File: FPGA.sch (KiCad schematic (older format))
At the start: 9 parts, among them U34 PCA9555AHF,128, U39 PCA9555AHF,128

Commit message: I2C voltage translator added, rotated POE bridges, I2C connected to SODIMM, NMOS for power leds indicator, 3V3P connected to SI570 and SODIMM
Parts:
- added C412, C415: CC0201_100NF_6.3V_10%_X5R, CAPC0603X33N, symbol Capacitors_SMD:CC0201_100NF_6.3V_10%_X5R
- added R25, R28: R0402_2K2_1%_0.0625W_100PPM, RESC1005X40N, symbol Resistors_SMD:R0402_2K2_1%_0.0625W_100PPM
- added U59: TCA9517DGKR, ICs And Semiconductors SMD:SOP65P490X110-8N, symbol Analog_&_Interface:TCA9517DGKR
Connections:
- net labels added: +3.3P, I2C_APP_3V3_SCL, I2C_APP_3V3_SDA
- wire segments 171 -> 187
- no-connect marks 12 -> 13

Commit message: More consistent attributes for LEDs and BSS138
Should match Marble-Mini
Fewer complaints from KiBoM
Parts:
- LD13, LD14: Manufacturer KINGBRIGHT -> WURTH; Manufacturer Part Number KPH-1608CGCK -> 150060VS75000
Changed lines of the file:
@@
 F 14 "~~" H 9750 8600 60  0001 L CNN "Status"
 F 15 "SMD Green LED, Case 1.6mmX0.8mm(0603), 0.65mm Thickness" H 9750 8510 60  0001 L CNN "Part Description"
-F 16 "KINGBRIGHT" H 9750 8420 60  0001 L CNN "Manufacturer"
-F 17 "KPH-1608CGCK" H 9750 8330 60  0001 L CNN "Manufacturer Part Number"
+F 16 "WURTH" H 9750 8420 60  0001 L CNN "Manufacturer"
+F 17 "150060VS75000" H 9750 8330 60  0001 L CNN "Manufacturer Part Number"
 F 18 "2" H 9750 8240 60  0001 L CNN "Pin Count"
 F 19 "~~" H 9750 8150 60  0001 L CNN "Case"
@@
 F 14 "~~" H 10100 8600 60  0001 L CNN "Status"
 F 15 "SMD Green LED, Case 1.6mmX0.8mm(0603), 0.65mm Thickness" H 10100 8510 60  0001 L CNN "Part Description"
-F 16 "KINGBRIGHT" H 10100 8420 60  0001 L CNN "Manufacturer"
-F 17 "KPH-1608CGCK" H 10100 8330 60  0001 L CNN "Manufacturer Part Number"
+F 16 "WURTH" H 10100 8420 60  0001 L CNN "Manufacturer"
+F 17 "150060VS75000" H 10100 8330 60  0001 L CNN "Manufacturer Part Number"
 F 18 "2" H 10100 8240 60  0001 L CNN "Pin Count"
 F 19 "~~" H 10100 8150 60  0001 L CNN "Case"

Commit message: Stop saying that 2-pin devices have "2.0000000000000000e+00" pins
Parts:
- C215, C342, C412, C415: Pin Count 2.0000000000000000e+00 -> 2
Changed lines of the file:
@@
 F 9 "Standard" H 1600 9260 60  0001 L CNN "Component Kind"
 F 10 "Standard" H 1600 9170 60  0001 L CNN "Component Type"
-F 11 "2.0000000000000000e+00" H 1600 8990 60  0001 L CNN "Pin Count"
+F 11 "2" H 1600 8990 60  0001 L CNN "Pin Count"
 F 12 "PcbLib\\Capacitors SMD.PcbLib" H 1600 8900 60  0001 L CNN "Footprint Path"
 F 13 "CAPC0603X33N" H 1600 8810 60  0001 L CNN "Footprint Ref"
@@
 F 9 "Standard" H 6750 9210 60  0001 L CNN "Component Kind"
 F 10 "Standard" H 6750 9120 60  0001 L CNN "Component Type"
-F 11 "2.0000000000000000e+00" H 6750 8940 60  0001 L CNN "Pin Count"
+F 11 "2" H 6750 8940 60  0001 L CNN "Pin Count"
 F 12 "PcbLib\\Capacitors SMD.PcbLib" H 6750 8850 60  0001 L CNN "Footprint Path"
 F 13 "CAPC0603X33N" H 6750 8760 60  0001 L CNN "Footprint Ref"
@@
 F 9 "Standard" H 12900 8010 60  0001 L CNN "Component Kind"
 F 10 "Standard" H 12900 7920 60  0001 L CNN "Component Type"
-F 11 "2.0000000000000000e+00" H 12900 7740 60  0001 L CNN "Pin Count"
+F 11 "2" H 12900 7740 60  0001 L CNN "Pin Count"
 F 12 "PcbLib\\Capacitors SMD.PcbLib" H 12900 7650 60  0001 L CNN "Footprint Path"
 F 13 "CAPC0603X33N" H 12900 7560 60  0001 L CNN "Footprint Ref"
@@
 F 9 "Standard" H 11550 7910 60  0001 L CNN "Component Kind"
 F 10 "Standard" H 11550 7820 60  0001 L CNN "Component Type"
-F 11 "2.0000000000000000e+00" H 11550 7640 60  0001 L CNN "Pin Count"
+F 11 "2" H 11550 7640 60  0001 L CNN "Pin Count"
 F 12 "PcbLib\\Capacitors SMD.PcbLib" H 11550 7550 60  0001 L CNN "Footprint Path"
 F 13 "CAPC0603X33N" H 11550 7460 60  0001 L CNN "Footprint Ref"

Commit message: Convert "~" and "~~" in .sch and .lib files to " "
cf. commit ef029e49 in Marble-Mini, May 21 2020
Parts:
- C215, C342, C412, C415: ComponentHeight ~~ -> (none); PackageDescription ~~ -> (none); PressFit ~~ -> (none); Sense Comment ~~ -> (none); Status Comment ~~ -> (none)
- LD13, LD14: Case ~~ -> (none); Comment ~~ -> (none); ComponentLink1Description ~~ -> (none); ComponentLink1URL ~~ -> (none); ComponentLink2Description ~~ -> (none); ComponentLink2URL ~~ -> (none); Device ~~ -> (none); Sense Comment ~~ -> (none); Status ~~ -> (none); Status Comment ~~ -> (none)
- R199, R25, R264, R265, R28: ComponentHeight ~~ -> (none); PackageDescription ~~ -> (none); Sense Comment ~~ -> (none); Status Comment ~~ -> (none); Voltage ~~ -> (none)
- U34, U39: ComponentLink1Description ~~ -> (none); ComponentLink1URL ~~ -> (none); ComponentLink2Description ~~ -> (none); ComponentLink2URL ~~ -> (none); Sense Comment ~~ -> (none); Status ~~ -> (none); Status Comment ~~ -> (none)

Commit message: Remove some un-helpful attributes
Pole4
SCEM
Footprint Library
Database Table Name
HelpURL
ComponentLink1URL
ComponentLink2URL
CreateDate1
LatestRevisionDate1

cf. commits 8f7a3695 c705ea46 d128e165 ffe4a47d in Marble-Mini, May 21 2020
Cuts number of attrib_lint complaints in half, to 2334.
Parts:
- C215, C342, C412, C415: HelpURL \\\\cern.ch\\dfs\\Applications\\Altium\\Datasheets\\CC0201_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 -> (none)
- LD13, LD14: ComponentLink1URL (none) -> (none); ComponentLink2URL (none) -> (none); HelpURL \\\\cern.ch\\dfs\\Applications\\Altium\\Datasheets\\LED_KIN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 -> (none); Pole4 Green -> (none)
- R199, R25, R264, R265, R28: HelpURL \\\\cern.ch\\dfs\\Applications\\Altium\\Datasheets\\R0402_P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 -> (none)
- U34, U39: ComponentLink1URL (none) -> (none); ComponentLink2URL (none) -> (none); HelpURL \\\\cern.ch\\dfs\\Applications\\Altium\\Datasheets\\PCA9555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 -> (none)
- U59: Database Table Name Analog & Interface -> (none); Footprint Library ICs And Semiconductors SMD -> (none); SCEM (none) -> (none)
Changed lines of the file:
@@
 F 28 "QFN50P400X400X80-25N-S225" H 7400 4340 60  0001 L CNN "Footprint Ref"
 F 29 "CERN DEM BC" H 7400 4250 60  0001 L CNN "Author"
-F 30 "\\\\cern.ch\\dfs\\Applications\\Altium\\Datasheets\\PCA9555AHF.pdf" H 7400 4160 60  0001 L CNN "HelpURL"
-F 31 " " H 7400 4070 60  0001 L CNN "ComponentLink1URL"
-F 32 " " H 7400 3980 60  0001 L CNN "ComponentLink2URL"
 F 33 " " H 7400 3890 60  0001 L CNN "ComponentLink2Description"
 F 34 " " H 7400 3800 60  0001 L CNN "ComponentLink1Description"
@@
 F 28 "QFN50P400X400X80-25N-S225" H 2650 4340 60  0001 L CNN "Footprint Ref"
 F 29 "CERN DEM BC" H 2650 4250 60  0001 L CNN "Author"
-F 30 "\\\\cern.ch\\dfs\\Applications\\Altium\\Datasheets\\PCA9555AHF.pdf" H 2650 4160 60  0001 L CNN "HelpURL"
-F 31 " " H 2650 4070 60  0001 L CNN "ComponentLink1URL"
-F 32 " " H 2650 3980 60  0001 L CNN "ComponentLink2URL"
 F 33 " " H 2650 3890 60  0001 L CNN "ComponentLink2Description"
 F 34 " " H 2650 3800 60  0001 L CNN "ComponentLink1Description"
@@
 F 33 "02016D104KAT2A" H 1600 7010 60  0001 L CNN "Manufacturer1 Part Number"
 F 34 "0.33mm" H 1600 6920 60  0001 L CNN "Manufacturer1 ComponentHeight"
-F 35 "\\\\cern.ch\\dfs\\Applications\\Altium\\Datasheets\\CC0201_X5R_AVX.pdf" H 1600 6830 60  0001 L CNN "HelpURL"
 F 36 "CERN DEM JLC" H 1600 6740 60  0001 L CNN "Author"
 F 37 "12/03/07 00:00:00" H 1600 6650 60  0001 L CNN "CreateDate"
@@
 F 33 "02016D104KAT2A" H 6750 6960 60  0001 L CNN "Manufacturer1 Part Number"
 F 34 "0.33mm" H 6750 6870 60  0001 L CNN "Manufacturer1 ComponentHeight"
-F 35 "\\\\cern.ch\\dfs\\Applications\\Altium\\Datasheets\\CC0201_X5R_AVX.pdf" H 6750 6780 60  0001 L CNN "HelpURL"
 F 36 "CERN DEM JLC" H 6750 6690 60  0001 L CNN "Author"
 F 37 "12/03/07 00:00:00" H 6750 6600 60  0001 L CNN "CreateDate"
@@
 F 34 "232270672202L" H 1300 5820 60  0001 L CNN "Manufacturer1 Part Number"
 F 35 "0.4mm" H 1300 5730 60  0001 L CNN "Manufacturer1 ComponentHeight"
-F 36 "\\\\cern.ch\\dfs\\Applications\\Altium\\Datasheets\\R0402_Phycomp_RC0402.pdf" H 1300 5640 60  0001 L CNN "HelpURL"
 F 37 "CERN DEM JLC" H 1300 5550 60  0001 L CNN "Author"
 F 38 "12/03/07 00:00:00" H 1300 5460 60  0001 L CNN "CreateDate"
@@
 F 34 "232270671002L" H 10100 6370 60  0001 L CNN "Manufacturer1 Part Number"
 F 35 "0.4mm" H 10100 6280 60  0001 L CNN "Manufacturer1 ComponentHeight"
-F 36 "\\\\cern.ch\\dfs\\Applications\\Altium\\Datasheets\\R0402_Phycomp_RC0402.pdf" H 10100 6190 60  0001 L CNN "HelpURL"
 F 37 "CERN DEM JLC" H 10100 6100 60  0001 L CNN "Author"
 F 38 "12/03/07 00:00:00" H 10100 6010 60  0001 L CNN "CreateDate"
@@
 F 34 "232270671002L" H 9750 6370 60  0001 L CNN "Manufacturer1 Part Number"
 F 35 "0.4mm" H 9750 6280 60  0001 L CNN "Manufacturer1 ComponentHeight"
-F 36 "\\\\cern.ch\\dfs\\Applications\\Altium\\Datasheets\\R0402_Phycomp_RC0402.pdf" H 9750 6190 60  0001 L CNN "HelpURL"
 F 37 "CERN DEM JLC" H 9750 6100 60  0001 L CNN "Author"
 F 38 "12/03/07 00:00:00" H 9750 6010 60  0001 L CNN "CreateDate"
@@
 F 2 "ICs And Semiconductors SMD:LED_KINGBRIGHT_KPH-1608CGCK" H 9750 8780 60  0001 L CNN
 F 3 "" H 9750 9590 60  0001 L CNN
-F 4 "Green" H 9750 9500 60  0001 L CNN "Pole4"
 F 5 "LED_KINGBRIGHT_KPH-1608CGCK" H 9750 9500 60  0001 L CNN "Part Number"
 F 6 "LED Green 1C 2A" H 9750 9410 60  0001 L CNN "Library Ref"
@@
 F 29 "PcbLib\\ICs And Semiconductors SMD.PcbLib" H 9750 7250 60  0001 L CNN "Footprint Path"
 F 30 "LED_KINGBRIGHT_KPH-1608CGCK" H 9750 7160 60  0001 L CNN "Footprint Ref"
-F 31 "\\\\cern.ch\\dfs\\Applications\\Altium\\Datasheets\\LED_KINGBRIGHT_KPH-1608CGCK.pdf" H 9750 7070 60  0001 L CNN "HelpURL"
-F 32 " " H 9750 6980 60  0001 L CNN "ComponentLink1URL"
 F 33 " " H 9750 6890 60  0001 L CNN "ComponentLink1Description"
-F 34 " " H 9750 6800 60  0001 L CNN "ComponentLink2URL"
 F 35 " " H 9750 6710 60  0001 L CNN "ComponentLink2Description"
 F 36 "CERN DEM JLC" H 9750 6620 60  0001 L CNN "Author"
@@
 F 2 "ICs And Semiconductors SMD:LED_KINGBRIGHT_KPH-1608CGCK" H 10100 8780 60  0001 L CNN
 F 3 "" H 10100 9590 60  0001 L CNN
-F 4 "Green" H 10100 9500 60  0001 L CNN "Pole4"
 F 5 "LED_KINGBRIGHT_KPH-1608CGCK" H 10100 9500 60  0001 L CNN "Part Number"
 F 6 "LED Green 1C 2A" H 10100 9410 60  0001 L CNN "Library Ref"
@@
 F 29 "PcbLib\\ICs And Semiconductors SMD.PcbLib" H 10100 7250 60  0001 L CNN "Footprint Path"
 F 30 "LED_KINGBRIGHT_KPH-1608CGCK" H 10100 7160 60  0001 L CNN "Footprint Ref"
-F 31 "\\\\cern.ch\\dfs\\Applications\\Altium\\Datasheets\\LED_KINGBRIGHT_KPH-1608CGCK.pdf" H 10100 7070 60  0001 L CNN "HelpURL"
-F 32 " " H 10100 6980 60  0001 L CNN "ComponentLink1URL"
 F 33 " " H 10100 6890 60  0001 L CNN "ComponentLink1Description"
-F 34 " " H 10100 6800 60  0001 L CNN "ComponentLink2URL"
 F 35 " " H 10100 6710 60  0001 L CNN "ComponentLink2Description"
 F 36 "CERN DEM JLC" H 10100 6620 60  0001 L CNN "Author"
@@
 F 32 "07/07/14 00:00:00" H 12700 5050 50  0001 L CNN "CreateDate"
 F 33 "07/07/14 00:00:00" H 12700 4975 50  0001 L CNN "LatestRevisionDate"
-F 34 " " H 12700 4900 50  0001 L CNN "SCEM"
-F 35 "Analog & Interface" H 12700 4825 50  0001 L CNN "Database Table Name"
 F 36 "ICs And Semiconductors.DbLib" H 12700 4750 50  0001 L CNN "Library Name"
-F 37 "ICs And Semiconductors SMD" H 12700 4675 50  0001 L CNN "Footprint Library"
 F 38 "This work is licensed under the Creative Commons CC-BY-SA 4.0 License. To the extent that circuit schematics that use Licensed Material can be considered to be ‘Adapted Material’, then the copyright holder waives article 3.b of the license with respect to these schematics." H 12700 4600 50  0001 L CNN "License"
 	1    12700 8250
@@
 F 33 "02016D104KAT2A" H 12900 5760 60  0001 L CNN "Manufacturer1 Part Number"
 F 34 "0.33mm" H 12900 5670 60  0001 L CNN "Manufacturer1 ComponentHeight"
-F 35 "\\\\cern.ch\\dfs\\Applications\\Altium\\Datasheets\\CC0201_X5R_AVX.pdf" H 12900 5580 60  0001 L CNN "HelpURL"
 F 36 "CERN DEM JLC" H 12900 5490 60  0001 L CNN "Author"
 F 37 "12/03/07 00:00:00" H 12900 5400 60  0001 L CNN "CreateDate"
@@
 F 33 "02016D104KAT2A" H 11550 5660 60  0001 L CNN "Manufacturer1 Part Number"
 F 34 "0.33mm" H 11550 5570 60  0001 L CNN "Manufacturer1 ComponentHeight"
-F 35 "\\\\cern.ch\\dfs\\Applications\\Altium\\Datasheets\\CC0201_X5R_AVX.pdf" H 11550 5480 60  0001 L CNN "HelpURL"
 F 36 "CERN DEM JLC" H 11550 5390 60  0001 L CNN "Author"
 F 37 "12/03/07 00:00:00" H 11550 5300 60  0001 L CNN "CreateDate"
@@
 F 34 "232270672202L" H 13200 4770 60  0001 L CNN "Manufacturer1 Part Number"
 F 35 "0.4mm" H 13200 4680 60  0001 L CNN "Manufacturer1 ComponentHeight"
-F 36 "\\\\cern.ch\\dfs\\Applications\\Altium\\Datasheets\\R0402_Phycomp_RC0402.pdf" H 13200 4590 60  0001 L CNN "HelpURL"
 F 37 "CERN DEM JLC" H 13200 4500 60  0001 L CNN "Author"
 F 38 "12/03/07 00:00:00" H 13200 4410 60  0001 L CNN "CreateDate"
@@
 F 34 "232270672202L" H 13000 4770 60  0001 L CNN "Manufacturer1 Part Number"
 F 35 "0.4mm" H 13000 4680 60  0001 L CNN "Manufacturer1 ComponentHeight"
-F 36 "\\\\cern.ch\\dfs\\Applications\\Altium\\Datasheets\\R0402_Phycomp_RC0402.pdf" H 13000 4590 60  0001 L CNN "HelpURL"
 F 37 "CERN DEM JLC" H 13000 4500 60  0001 L CNN "Author"
 F 38 "12/03/07 00:00:00" H 13000 4410 60  0001 L CNN "CreateDate"

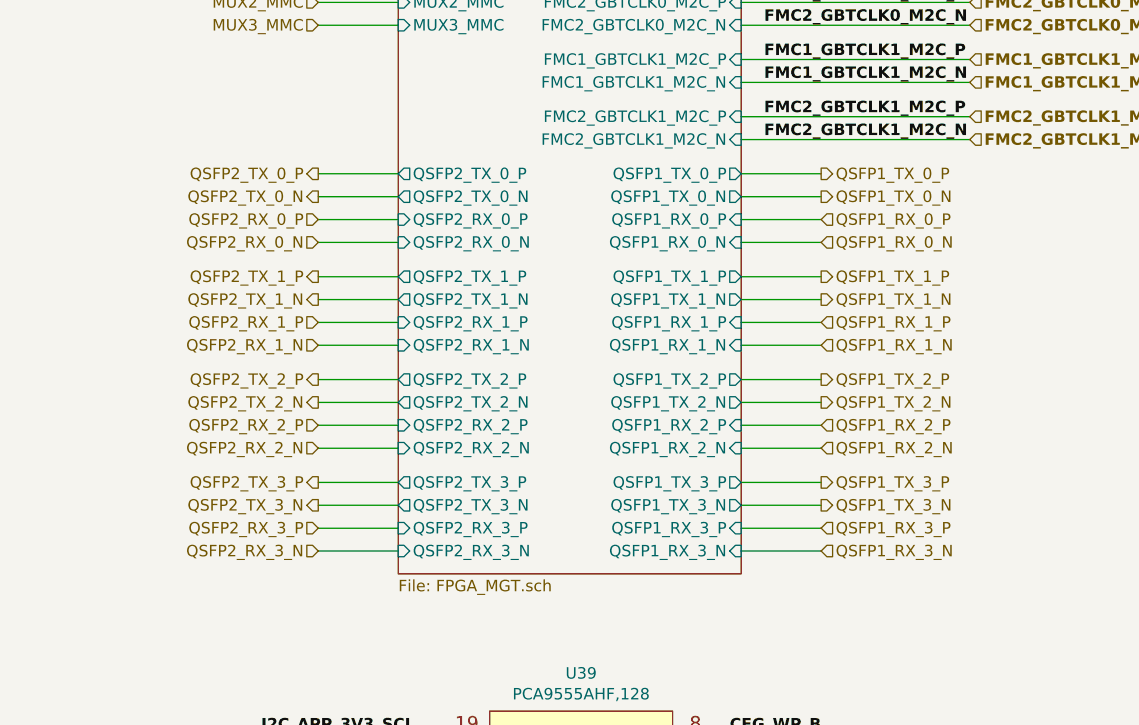
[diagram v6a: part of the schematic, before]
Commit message: Remap QSFP lane netnames for less confusion
All now agree with 1,2,3,4 labels on QSFP connector
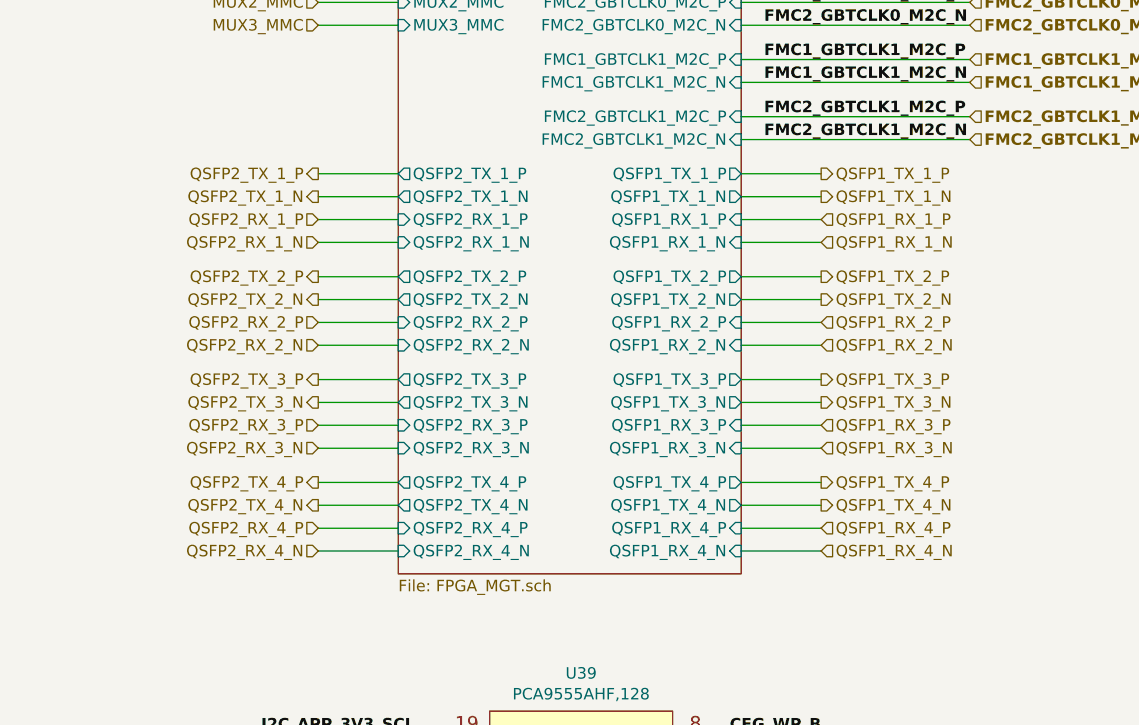
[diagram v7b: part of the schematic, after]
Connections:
- net labels added: QSFP1_RX_4_N, QSFP1_RX_4_P, QSFP1_TX_4_N, QSFP1_TX_4_P, QSFP2_RX_4_N, QSFP2_RX_4_P, QSFP2_TX_4_N, QSFP2_TX_4_P
- net labels removed: QSFP1_RX_0_N, QSFP1_RX_0_P, QSFP1_TX_0_N, QSFP1_TX_0_P, QSFP2_RX_0_N, QSFP2_RX_0_P, QSFP2_TX_0_N, QSFP2_TX_0_P
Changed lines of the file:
@@
 	3650 10250 4500 10250
 Text HLabel 8850 6500 2    50   Output ~ 0
-QSFP1_TX_0_P
+QSFP1_TX_1_P
 Text HLabel 8850 6600 2    50   Output ~ 0
-QSFP1_TX_0_N
+QSFP1_TX_1_N
 Text HLabel 8850 6700 2    50   Input ~ 0
-QSFP1_RX_0_P
+QSFP1_RX_1_P
 Text HLabel 8850 6800 2    50   Input ~ 0
-QSFP1_RX_0_N
+QSFP1_RX_1_N
 Text HLabel 8850 6950 2    50   Output ~ 0
-QSFP1_TX_1_P
+QSFP1_TX_2_P
 Text HLabel 8850 7050 2    50   Output ~ 0
-QSFP1_TX_1_N
+QSFP1_TX_2_N
 Text HLabel 8850 7150 2    50   Input ~ 0
-QSFP1_RX_1_P
+QSFP1_RX_2_P
 Text HLabel 8850 7250 2    50   Input ~ 0
-QSFP1_RX_1_N
+QSFP1_RX_2_N
 Text HLabel 8850 7400 2    50   Output ~ 0
-QSFP1_TX_2_P
+QSFP1_TX_3_P
 Text HLabel 8850 7500 2    50   Output ~ 0
-QSFP1_TX_2_N
+QSFP1_TX_3_N
 Text HLabel 8850 7600 2    50   Input ~ 0
-QSFP1_RX_2_P
+QSFP1_RX_3_P
 Text HLabel 8850 7700 2    50   Input ~ 0
-QSFP1_RX_2_N
+QSFP1_RX_3_N
 Text HLabel 8850 7850 2    50   Output ~ 0
-QSFP1_TX_3_P
+QSFP1_TX_4_P
 Text HLabel 8850 7950 2    50   Output ~ 0
-QSFP1_TX_3_N
+QSFP1_TX_4_N
 Text HLabel 8850 8050 2    50   Input ~ 0
-QSFP1_RX_3_P
+QSFP1_RX_4_P
 Text HLabel 8850 8150 2    50   Input ~ 0
-QSFP1_RX_3_N
+QSFP1_RX_4_N
 Text HLabel 6650 6500 0    50   Output ~ 0
-QSFP2_TX_0_P
+QSFP2_TX_1_P
 Text HLabel 6650 6600 0    50   Output ~ 0
-QSFP2_TX_0_N
+QSFP2_TX_1_N
 Text HLabel 6650 6700 0    50   Input ~ 0
-QSFP2_RX_0_P
+QSFP2_RX_1_P
 Text HLabel 6650 6800 0    50   Input ~ 0
-QSFP2_RX_0_N
+QSFP2_RX_1_N
 Text HLabel 6650 6950 0    50   Output ~ 0
-QSFP2_TX_1_P
+QSFP2_TX_2_P
 Text HLabel 6650 7050 0    50   Output ~ 0
-QSFP2_TX_1_N
+QSFP2_TX_2_N
 Text HLabel 6650 7150 0    50   Input ~ 0
-QSFP2_RX_1_P
+QSFP2_RX_2_P
 Text HLabel 6650 7250 0    50   Input ~ 0
-QSFP2_RX_1_N
+QSFP2_RX_2_N
 Text HLabel 6650 7400 0    50   Output ~ 0
-QSFP2_TX_2_P
+QSFP2_TX_3_P
 Text HLabel 6650 7500 0    50   Output ~ 0
-QSFP2_TX_2_N
+QSFP2_TX_3_N
 Text HLabel 6650 7600 0    50   Input ~ 0
-QSFP2_RX_2_P
+QSFP2_RX_3_P
 Text HLabel 6650 7700 0    50   Input ~ 0
-QSFP2_RX_2_N
+QSFP2_RX_3_N
 Text HLabel 6650 7850 0    50   Output ~ 0
-QSFP2_TX_3_P
+QSFP2_TX_4_P
 Text HLabel 6650 7950 0    50   Output ~ 0
-QSFP2_TX_3_N
+QSFP2_TX_4_N
 Text HLabel 6650 8050 0    50   Input ~ 0
-QSFP2_RX_3_P
+QSFP2_RX_4_P
 Text HLabel 6650 8150 0    50   Input ~ 0
-QSFP2_RX_3_N
+QSFP2_RX_4_N
 Wire Wire Line
 	6650 6500 7000 6500
@@
 F12 "FMC2_GBTCLK1_M2C_P" I R 8500 6250 50
 F13 "FMC2_GBTCLK1_M2C_N" I R 8500 6350 50
-F14 "QSFP2_TX_0_P" O L 7000 6500 50
-F15 "QSFP2_TX_0_N" O L 7000 6600 50
-F16 "QSFP2_RX_0_P" I L 7000 6700 50
-F17 "QSFP2_RX_0_N" I L 7000 6800 50
-F18 "QSFP2_TX_1_P" O L 7000 6950 50
-F19 "QSFP2_TX_1_N" O L 7000 7050 50
-F20 "QSFP2_RX_1_P" I L 7000 7150 50
-F21 "QSFP2_RX_1_N" I L 7000 7250 50
-F22 "QSFP2_TX_2_P" O L 7000 7400 50
-F23 "QSFP2_TX_2_N" O L 7000 7500 50
-F24 "QSFP2_RX_2_P" I L 7000 7600 50
-F25 "QSFP2_RX_2_N" I L 7000 7700 50
-F26 "QSFP2_TX_3_P" O L 7000 7850 50
-F27 "QSFP2_TX_3_N" O L 7000 7950 50
-F28 "QSFP2_RX_3_P" I L 7000 8050 50
-F29 "QSFP2_RX_3_N" I L 7000 8150 50
-F30 "QSFP1_TX_0_P" O R 8500 6500 50
-F31 "QSFP1_TX_0_N" O R 8500 6600 50
-F32 "QSFP1_RX_0_P" I R 8500 6700 50
-F33 "QSFP1_RX_0_N" I R 8500 6800 50
-F34 "QSFP1_TX_1_P" O R 8500 6950 50
-F35 "QSFP1_TX_1_N" O R 8500 7050 50
-F36 "QSFP1_RX_1_P" I R 8500 7150 50
-F37 "QSFP1_RX_1_N" I R 8500 7250 50
-F38 "QSFP1_TX_2_P" O R 8500 7400 50
-F39 "QSFP1_TX_2_N" O R 8500 7500 50
-F40 "QSFP1_RX_2_P" I R 8500 7600 50
-F41 "QSFP1_RX_2_N" I R 8500 7700 50
-F42 "QSFP1_TX_3_P" O R 8500 7850 50
-F43 "QSFP1_TX_3_N" O R 8500 7950 50
-F44 "QSFP1_RX_3_P" I R 8500 8050 50
-F45 "QSFP1_RX_3_N" I R 8500 8150 50
+F14 "QSFP2_TX_1_P" O L 7000 6500 50
+F15 "QSFP2_TX_1_N" O L 7000 6600 50
+F16 "QSFP2_RX_1_P" I L 7000 6700 50
+F17 "QSFP2_RX_1_N" I L 7000 6800 50
+F18 "QSFP2_TX_2_P" O L 7000 6950 50
+F19 "QSFP2_TX_2_N" O L 7000 7050 50
+F20 "QSFP2_RX_2_P" I L 7000 7150 50
+F21 "QSFP2_RX_2_N" I L 7000 7250 50
+F22 "QSFP2_TX_3_P" O L 7000 7400 50
+F23 "QSFP2_TX_3_N" O L 7000 7500 50
+F24 "QSFP2_RX_3_P" I L 7000 7600 50
+F25 "QSFP2_RX_3_N" I L 7000 7700 50
+F26 "QSFP2_TX_4_P" O L 7000 7850 50
+F27 "QSFP2_TX_4_N" O L 7000 7950 50
+F28 "QSFP2_RX_4_P" I L 7000 8050 50
+F29 "QSFP2_RX_4_N" I L 7000 8150 50
+F30 "QSFP1_TX_1_P" O R 8500 6500 50
+F31 "QSFP1_TX_1_N" O R 8500 6600 50
+F32 "QSFP1_RX_1_P" I R 8500 6700 50
+F33 "QSFP1_RX_1_N" I R 8500 6800 50
+F34 "QSFP1_TX_2_P" O R 8500 6950 50
+F35 "QSFP1_TX_2_N" O R 8500 7050 50
+F36 "QSFP1_RX_2_P" I R 8500 7150 50
+F37 "QSFP1_RX_2_N" I R 8500 7250 50
+F38 "QSFP1_TX_3_P" O R 8500 7400 50
+F39 "QSFP1_TX_3_N" O R 8500 7500 50
+F40 "QSFP1_RX_3_P" I R 8500 7600 50
+F41 "QSFP1_RX_3_N" I R 8500 7700 50
+F42 "QSFP1_TX_4_P" O R 8500 7850 50
+F43 "QSFP1_TX_4_N" O R 8500 7950 50
+F44 "QSFP1_RX_4_P" I R 8500 8050 50
+F45 "QSFP1_RX_4_N" I R 8500 8150 50
 F46 "CLKMUX_RST" I L 7000 5450 50
 F47 "MUX1_MMC" I L 7000 5650 50
